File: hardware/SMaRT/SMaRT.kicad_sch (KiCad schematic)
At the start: 17 parts, among them J1 Glider, J10 Conn_01x08, J11 Conn_01x08, J12 Qwiic_Connector, J2 Sensor, J3 TestPins_Glider, J4 TestPins_Sensor, J5 Programmer, J6 Conn_01x03, J7 Conn_01x04, J8 Conn_01x04, J9 Conn_01x06, U2 MAX3232_SPARKFUN, U3 MAX3232_SPARKFUN

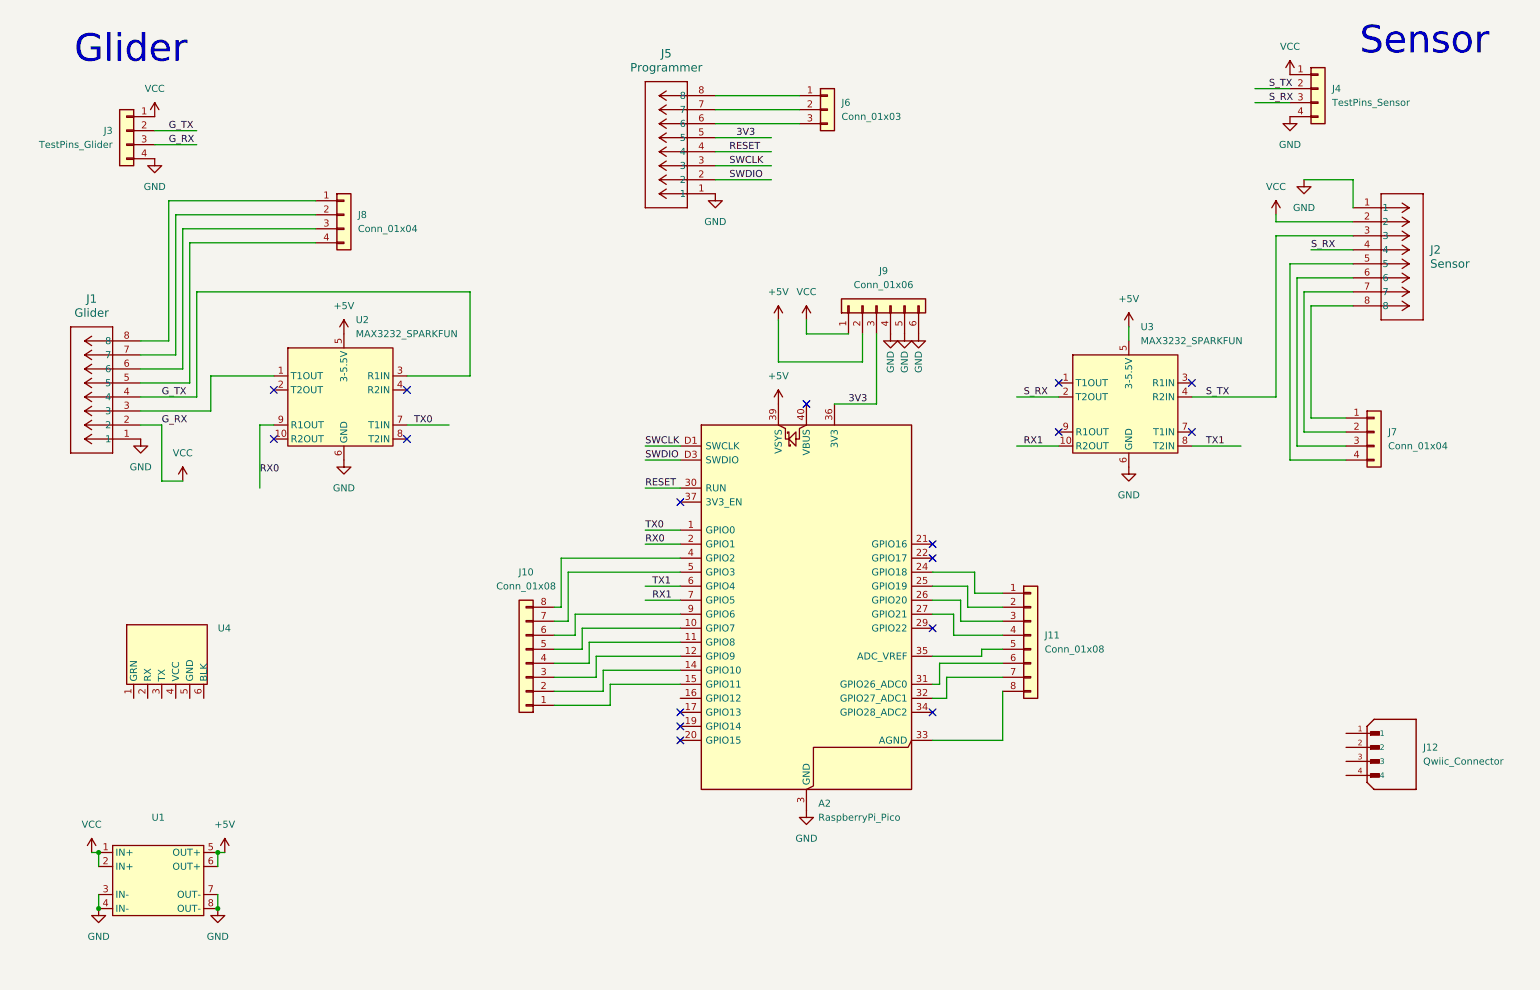
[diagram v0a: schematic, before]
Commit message: added openlog, relay, switch
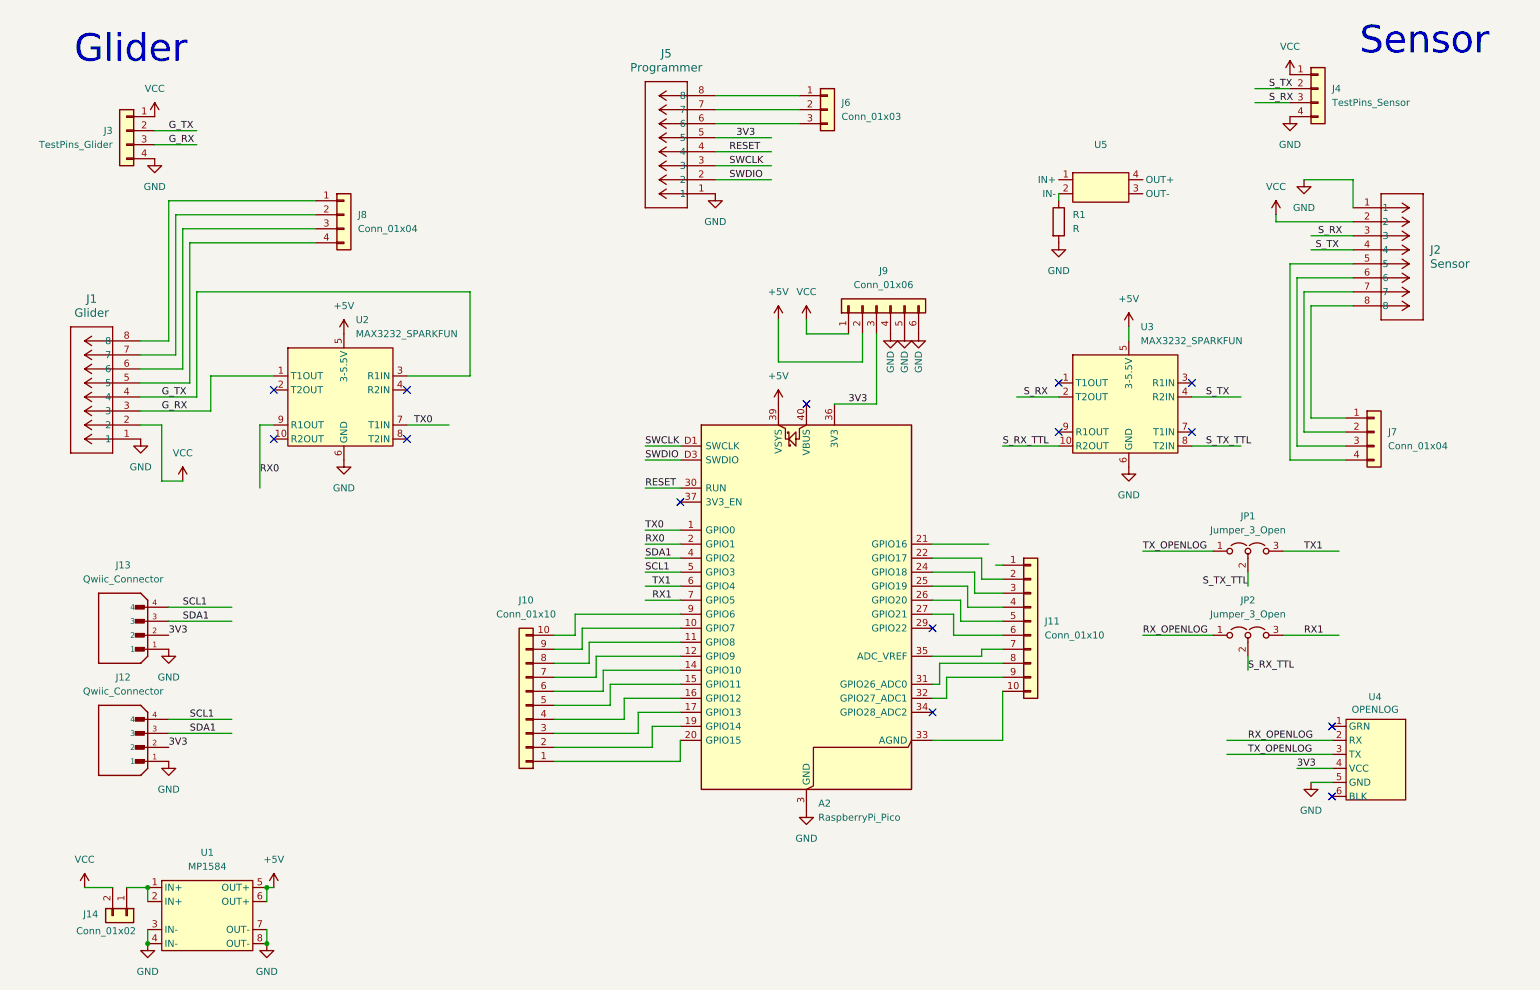
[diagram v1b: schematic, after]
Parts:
- removed J10, J11: Conn_01x08, Connector_PinHeader_2.54mm:PinHeader_1x08_P2.54mm_Vertical, symbol Connector_Generic:Conn_01x08
- added J10, J11: Conn_01x10, Connector_PinHeader_2.54mm:PinHeader_1x10_P2.54mm_Vertical, symbol Connector_Generic:Conn_01x10
- added J13: Qwiic_Connector, Qwiic:Qwiic, symbol Qwiic:Qwiic_Connector
- added J14: Conn_01x02, Connector_PinHeader_2.54mm:PinHeader_1x02_P2.54mm_Vertical, symbol Connector_Generic:Conn_01x02
- added JP1, JP2: Jumper_3_Open, Connector_PinHeader_2.54mm:PinHeader_1x03_P2.54mm_Vertical, symbol Jumper:Jumper_3_Open
- added R1: R, symbol Device:R
- added U5: ~, symbol SSR:U_1
- J12: footprint PRT-14417:SPARKFUN_PRT-14417 -> Qwiic:Qwiic
- J6: footprint Connector_PinHeader_2.54mm:PinHeader_1x04_P2.54mm_Vertical -> Connector_PinHeader_2.54mm:PinHeader_1x03_P2.54mm_Vertical
- U1: value ~ -> MP1584; footprint (none) -> MPT1684:MPT1584EN_Module
- U4: value ~ -> OPENLOG; footprint (none) -> OpenLog:OpenLog
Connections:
- net 3V3: now also J12.2, U4.4 (VCC), J13.2
- net GND: now also J12.1, U4.5 (GND), J13.1, R1.2
- net RX1: now also JP2.3 (B); no longer U3.10 (R2OUT)
- net S_RX: now also J2.3; no longer J2.4
- net S_TX: now also J2.4; no longer J2.3
- net TX1: now also JP1.3 (B); no longer U3.8 (T2IN)
- net VCC: now also J14.2 (Pin_2); no longer J3.3 (Pin_3), U1.1 (IN+), U1.2 (IN+)
- net at A2.15 (GPIO11): now also J10.5 (Pin_5)
- net at A2.14 (GPIO10): now also J10.6 (Pin_6)
- net at A2.12 (GPIO9): now also J10.7 (Pin_7)
- net at A2.11 (GPIO8): now also J10.8 (Pin_8)
- net at A2.10 (GPIO7): now also J10.9 (Pin_9)
- net at A2.9 (GPIO6): now also J10.10 (Pin_10)
- net SCL1: now reaches A2.5 (GPIO3)
- net SCL1: now also J12.4, J13.4
- net SDA1: now reaches A2.4 (GPIO2)
- net SDA1: now also J12.3, J13.3
- net G_RX: now reaches J1.3, U2.1 (T1OUT)
- net G_RX: now also J3.3 (Pin_3)
- net at A2.24 (GPIO18): now also J11.3 (Pin_3)
- net at A2.25 (GPIO19): now also J11.4 (Pin_4)
- net at A2.26 (GPIO20): now also J11.5 (Pin_5)
- net at A2.27 (GPIO21): now also J11.6 (Pin_6)
- net at A2.35 (ADC_VREF): now also J11.7 (Pin_7)
- net at A2.31 (GPIO26_ADC0): now also J11.8 (Pin_8)
- net at A2.32 (GPIO27_ADC1): now also J11.9 (Pin_9)
- net at A2.33 (AGND): now also J11.10 (Pin_10)
- net RX_OPENLOG: now reaches U4.2 (RX)
- net RX_OPENLOG: now also JP2.1 (A)
- net TX_OPENLOG: now reaches U4.3 (TX)
- net TX_OPENLOG: now also JP1.1 (A)
- net at A2.16 (GPIO12): now also J10.4 (Pin_4)
- net at A2.17 (GPIO13): now also J10.3 (Pin_3)
- net at A2.19 (GPIO14): now also J10.2 (Pin_2)
- net at A2.20 (GPIO15): now also J10.1 (Pin_1)
- net at A2.22 (GPIO17): now also J11.2 (Pin_2)
- new net: J14.1 (Pin_1), U1.1 (IN+), U1.2 (IN+)
- new net S_RX_TTL: JP2.2 (C), U3.10 (R2OUT)
- new net S_TX_TTL: JP1.2 (C), U3.8 (T2IN)
- no-connect marks 17 -> 14
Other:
- moved on the sheet: J12, U1, U4

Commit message: relay addition
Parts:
- added JP3: Jumper_3_Open, Connector_PinHeader_2.54mm:PinHeader_1x03_P2.54mm_Vertical, symbol Jumper:Jumper_3_Open
- R1: footprint (none) -> Resistor_THT:R_Axial_DIN0207_L6.3mm_D2.5mm_P7.62mm_Horizontal
- U5: footprint (none) -> G3VM-41AY1:G3VM-41AY1
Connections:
- net GND: now also U5.3 (OUT-), JP3.3 (B); no longer J2.1
- net RELAY: now reaches U5.1 (IN+)
- net RELAY: now also A2.21 (GPIO16)
- net at U5.2 (IN-): now also R1.1
- net at U5.4 (OUT+): now also JP3.1 (A)
- net at J11.1 (Pin_1): now also A2.22 (GPIO17)
- net at J11.2 (Pin_2): now also A2.24 (GPIO18); no longer A2.22 (GPIO17)
- net at J11.3 (Pin_3): now also A2.25 (GPIO19); no longer A2.24 (GPIO18)
- net at J11.4 (Pin_4): now also A2.26 (GPIO20); no longer A2.25 (GPIO19)
- net at J11.5 (Pin_5): now also A2.27 (GPIO21); no longer A2.26 (GPIO20)
- net at J11.6 (Pin_6): now also A2.29 (GPIO22); no longer A2.27 (GPIO21)
- new net: J2.1, JP3.2 (C)
- no-connect marks 14 -> 13
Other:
- moved on the sheet: R1, U5

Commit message: hardware: update SMaRT board and ignore KiCad artifacts
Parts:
- J13: renamed from J2; footprint Library:CONN_2068320000-SD_08_MOL -> MolexLib:CONN_2068320000-SD_08_MOL
- J5: renamed from J1; footprint Library:CONN_2068320000-SD_08_MOL -> MolexLib:CONN_2068320000-SD_08_MOL
- J8: renamed from J5; footprint Library:CONN_2068320000-SD_08_MOL -> MolexLib:CONN_2068320000-SD_08_MOL
- renumbered A2 to A1, J3 to J1, J9 to J10, J4 to J12, J7 to J14, J13 to J2, J12 to J3, J14 to J4, J8 to J6, J10 to J7, J6 to J9, JP3 to JP1, JP1 to JP2, JP2 to JP3, U5 to U3, U3 to U4, U4 to U5

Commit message: hardware: update PCB and schematic
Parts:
- J10: value Conn_01x06 -> Power_TP
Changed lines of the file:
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@@
 		)
 		(instances
-			(project ""
+			(project "SMaRT"
 				(path "/9c744ed5-e38b-4f2d-8eb3-155f8a60c9bf"
 					(reference "#PWR012")
@@
 		)
 		(instances
-			(project ""
+			(project "SMaRT"
 				(path "/9c744ed5-e38b-4f2d-8eb3-155f8a60c9bf"
 					(reference "J9")
@@
 		)
 		(instances
-			(project ""
+			(project "SMaRT"
 				(path "/9c744ed5-e38b-4f2d-8eb3-155f8a60c9bf"
 					(reference "U1")
@@
 		)
 		(instances
-			(project ""
+			(project "SMaRT"
 				(path "/9c744ed5-e38b-4f2d-8eb3-155f8a60c9bf"
 					(reference "#PWR09")
@@
 		)
 		(instances
-			(project ""
+			(project "SMaRT"
 				(path "/9c744ed5-e38b-4f2d-8eb3-155f8a60c9bf"
 					(reference "#PWR04")
@@
 		)
 		(instances
-			(project ""
+			(project "SMaRT"
 				(path "/9c744ed5-e38b-4f2d-8eb3-155f8a60c9bf"
 					(reference "J6")
@@
 		)
 		(instances
-			(project ""
+			(project "SMaRT"
 				(path "/9c744ed5-e38b-4f2d-8eb3-155f8a60c9bf"
 					(reference "U4")
@@
 		)
 		(instances
-			(project ""
+			(project "SMaRT"
 				(path "/9c744ed5-e38b-4f2d-8eb3-155f8a60c9bf"
 					(reference "U3")
@@
 		)
 		(instances
-			(project ""
+			(project "SMaRT"
 				(path "/9c744ed5-e38b-4f2d-8eb3-155f8a60c9bf"
 					(reference "#PWR015")
@@
 		)
 		(instances
-			(project ""
+			(project "SMaRT"
 				(path "/9c744ed5-e38b-4f2d-8eb3-155f8a60c9bf"
 					(reference "J11")
@@
 		)
 		(instances
-			(project ""
+			(project "SMaRT"
 				(path "/9c744ed5-e38b-4f2d-8eb3-155f8a60c9bf"
 					(reference "J5")
@@
 		)
 		(instances
-			(project ""
+			(project "SMaRT"
 				(path "/9c744ed5-e38b-4f2d-8eb3-155f8a60c9bf"
 					(reference "J3")
@@
 		)
 		(instances
-			(project ""
+			(project "SMaRT"
 				(path "/9c744ed5-e38b-4f2d-8eb3-155f8a60c9bf"
 					(reference "#PWR024")
@@
 		)
 		(instances
-			(project ""
+			(project "SMaRT"
 				(path "/9c744ed5-e38b-4f2d-8eb3-155f8a60c9bf"
 					(reference "R1")
@@
 		)
 		(instances
-			(project ""
+			(project "SMaRT"
 				(path "/9c744ed5-e38b-4f2d-8eb3-155f8a60c9bf"
 					(reference "J4")
@@
 		)
 		(instances
-			(project ""
+			(project "SMaRT"
 				(path "/9c744ed5-e38b-4f2d-8eb3-155f8a60c9bf"
 					(reference "#PWR06")
@@
 		)
 		(instances
-			(project ""
+			(project "SMaRT"
 				(path "/9c744ed5-e38b-4f2d-8eb3-155f8a60c9bf"
 					(reference "J7")
@@
 		)
 		(instances
-			(project ""
+			(project "SMaRT"
 				(path "/9c744ed5-e38b-4f2d-8eb3-155f8a60c9bf"
 					(reference "#PWR028")
@@
 		)
 		(instances
-			(project ""
+			(project "SMaRT"
 				(path "/9c744ed5-e38b-4f2d-8eb3-155f8a60c9bf"
 					(reference "#PWR027")
@@
 		)
 		(instances
-			(project ""
+			(project "SMaRT"
 				(path "/9c744ed5-e38b-4f2d-8eb3-155f8a60c9bf"
 					(reference "#PWR017")
@@
 		)
 		(instances
-			(project ""
+			(project "SMaRT"
 				(path "/9c744ed5-e38b-4f2d-8eb3-155f8a60c9bf"
 					(reference "JP2")
@@
 		)
 		(instances
-			(project ""
+			(project "SMaRT"
 				(path "/9c744ed5-e38b-4f2d-8eb3-155f8a60c9bf"
 					(reference "#PWR011")
@@
 		)
 		(instances
-			(project ""
+			(project "SMaRT"
 				(path "/9c744ed5-e38b-4f2d-8eb3-155f8a60c9bf"
 					(reference "#PWR010")
@@
 		)
 		(instances
-			(project ""
+			(project "SMaRT"
 				(path "/9c744ed5-e38b-4f2d-8eb3-155f8a60c9bf"
 					(reference "#PWR023")
@@
 		)
 		(instances
-			(project ""
+			(project "SMaRT"
 				(path "/9c744ed5-e38b-4f2d-8eb3-155f8a60c9bf"
 					(reference "#PWR025")
@@
 		)
 		(instances
-			(project ""
+			(project "SMaRT"
 				(path "/9c744ed5-e38b-4f2d-8eb3-155f8a60c9bf"
 					(reference "#PWR026")
@@
 		)
 		(instances
-			(project ""
+			(project "SMaRT"
 				(path "/9c744ed5-e38b-4f2d-8eb3-155f8a60c9bf"
 					(reference "#PWR014")
@@
 			)
 		)
-		(property "Value" "Conn_01x06"
+		(property "Value" "Power_TP"
 			(at 168.91 64.77 90)
 			(effects
@@
 		)
 		(instances
-			(project ""
+			(project "SMaRT"
 				(path "/9c744ed5-e38b-4f2d-8eb3-155f8a60c9bf"
 					(reference "J10")
@@
 		)
 		(instances
-			(project ""
+			(project "SMaRT"
 				(path "/9c744ed5-e38b-4f2d-8eb3-155f8a60c9bf"
 					(reference "#PWR08")
@@
 		)
 		(instances
-			(project ""
+			(project "SMaRT"
 				(path "/9c744ed5-e38b-4f2d-8eb3-155f8a60c9bf"
 					(reference "U2")
@@
 		)
 		(instances
-			(project ""
+			(project "SMaRT"
 				(path "/9c744ed5-e38b-4f2d-8eb3-155f8a60c9bf"
 					(reference "J13")
@@
 		)
 		(instances
-			(project ""
+			(project "SMaRT"
 				(path "/9c744ed5-e38b-4f2d-8eb3-155f8a60c9bf"
 					(reference "#PWR01")
@@
 		)
 		(instances
-			(project ""
+			(project "SMaRT"
 				(path "/9c744ed5-e38b-4f2d-8eb3-155f8a60c9bf"
 					(reference "U5")
@@
 		)
 		(instances
-			(project ""
+			(project "SMaRT"
 				(path "/9c744ed5-e38b-4f2d-8eb3-155f8a60c9bf"
 					(reference "J12")
@@
 		)
 		(instances
-			(project ""
+			(project "SMaRT"
 				(path "/9c744ed5-e38b-4f2d-8eb3-155f8a60c9bf"
 					(reference "#PWR03")
@@
 		)
 		(instances
-			(project ""
+			(project "SMaRT"
 				(path "/9c744ed5-e38b-4f2d-8eb3-155f8a60c9bf"
 					(reference "#PWR05")
@@
 		)
 		(instances
-			(project ""
+			(project "SMaRT"
 				(path "/9c744ed5-e38b-4f2d-8eb3-155f8a60c9bf"
 					(reference "A1")
@@
 		)
 		(instances
-			(project ""
+			(project "SMaRT"
 				(path "/9c744ed5-e38b-4f2d-8eb3-155f8a60c9bf"
 					(reference "#PWR02")

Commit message: First version of the SMaRT cabling
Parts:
- U3: value ~ -> (none)
